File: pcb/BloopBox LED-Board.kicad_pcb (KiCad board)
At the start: 2 copper layers, 25 x 15 mm, 4 parts, among them J1 Mainboard

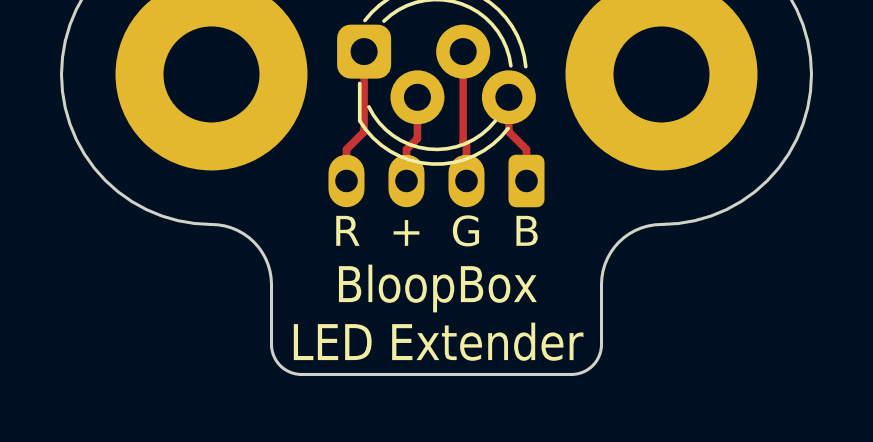
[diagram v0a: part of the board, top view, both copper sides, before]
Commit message: feat: add and use versioning variables
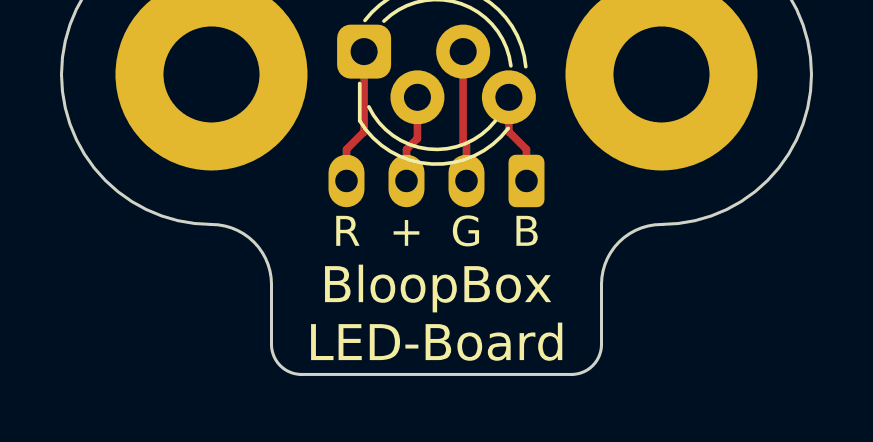
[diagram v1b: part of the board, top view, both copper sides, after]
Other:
- board text added: "BloopBox LED-Board"
- board text removed: "BloopBox LED Extender"
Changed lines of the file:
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@@
   (title_block
     (title "BloopBox LED-Board")
-    (date "2022-12-01")
-    (rev "1.0")
+    (date "${DATE}")
+    (rev "${VERSION}")
     (company "Qetesh")
   )
@@
     )
   )
+  (property "DATE" "~DATE~")
+  (property "VERSION" "~VERSION~")
   (net 0 "")
   (net 1 "/R")
@@
     (effects (font (size 1 1) (thickness 0.15)))
   )
-  (gr_text "BloopBox\nLED Extender" (at 150 108) (layer "F.SilkS")
-    (effects (font (size 1.2 1.05) (thickness 0.2)))
+  (gr_text "BloopBox\nLED-Board" (at 150 108) (layer "F.SilkS")
+    (effects (font (size 1.2 1.2) (thickness 0.2)))
   )
   (gr_text "R" (at 147 105.25) (layer "F.SilkS")

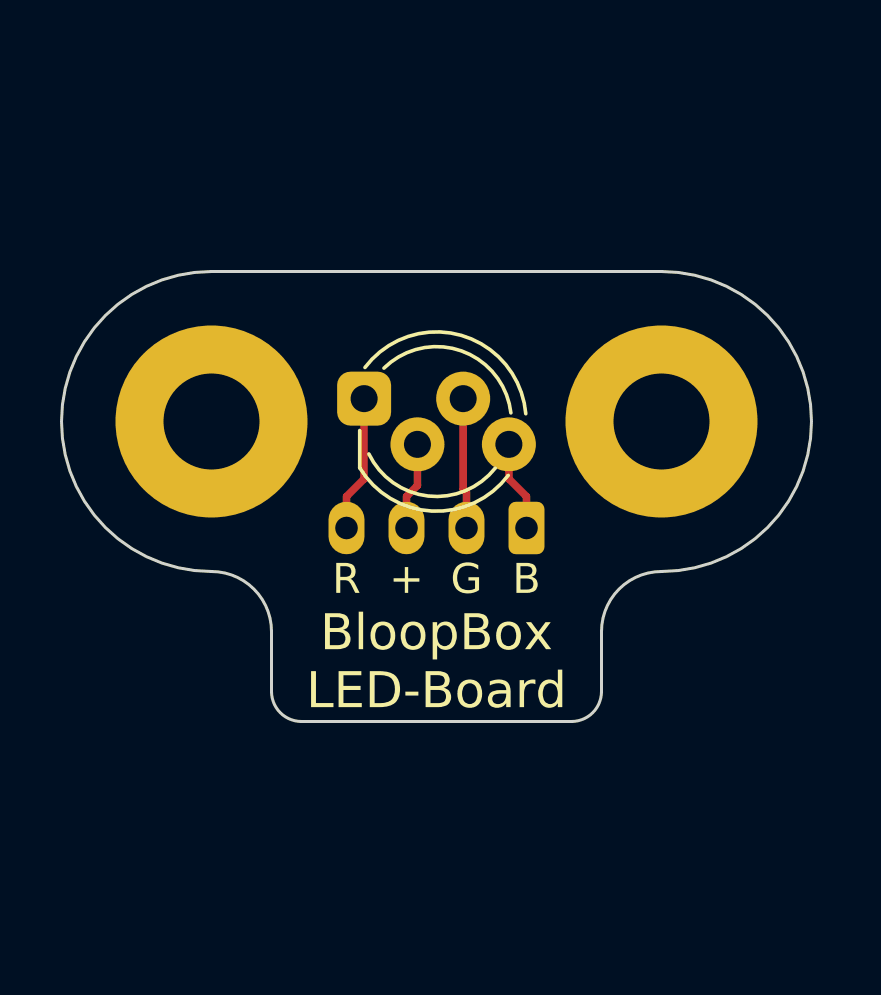
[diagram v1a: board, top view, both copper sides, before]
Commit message: feat: add breakaway rails to pcb
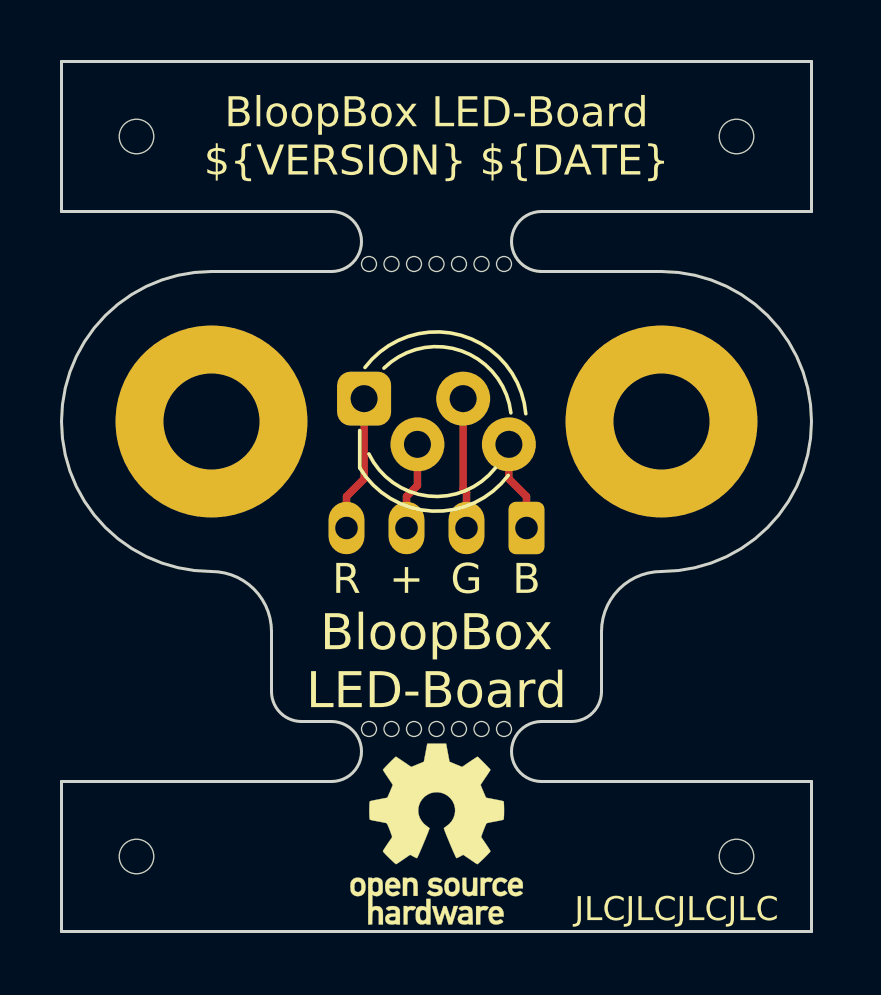
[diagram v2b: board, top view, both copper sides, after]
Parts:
- added G***: LOGO, My_Footprints:CutieMark5mmInverted, B.Cu at (150.0, 113.0)
- added REF**: JLCPCB_Tooling_Hole, My_Footprints:JLCPCB_Tooling_Hole, F.Cu at (160.0, 90.5)
- added REF**: JLCPCB_Tooling_Hole, My_Footprints:JLCPCB_Tooling_Hole, F.Cu at (140.0, 90.5)
- added REF**: JLCPCB_Tooling_Hole, My_Footprints:JLCPCB_Tooling_Hole, F.Cu at (140.0, 114.5)
- added REF**: JLCPCB_Tooling_Hole, My_Footprints:JLCPCB_Tooling_Hole, F.Cu at (160.0, 114.5)
- added REF**: OSHW-Logo_5.7x6mm_SilkScreen, Symbol:OSHW-Logo_5.7x6mm_SilkScreen, F.Cu at (150.0, 113.8)
- added mouse-bite-2mm-slot: VAL**, Panelization:mouse-bite-2x5mm-slot-onesided, F.Cu at (150.0, 94.0)
- added mouse-bite-2mm-slot: VAL**, Panelization:mouse-bite-2x5mm-slot-onesided, F.Cu at (150.0, 111.0)
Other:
- board size 25 x 15 mm -> 25 x 29 mm
- board text added: "${TITLE} ${VERSION} ${DATE}"
- board text added: "JLCJLCJLCJLC"
- board text added: "qete.sh/el"
